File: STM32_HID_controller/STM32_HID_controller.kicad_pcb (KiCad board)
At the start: 2 copper layers, 237.3 x 103.7 mm, 48 parts, among them J1 USB_B_Micro, J2 Conn_01x04_Pin, J3 Conn_01x03_Pin, J5 Conn_01x03_Pin, SW1 SW_SPDT, SW10 SW_Push, SW11 SW_Push, SW14 SW_Push, SW2 SW_Push, SW3 SW_Push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

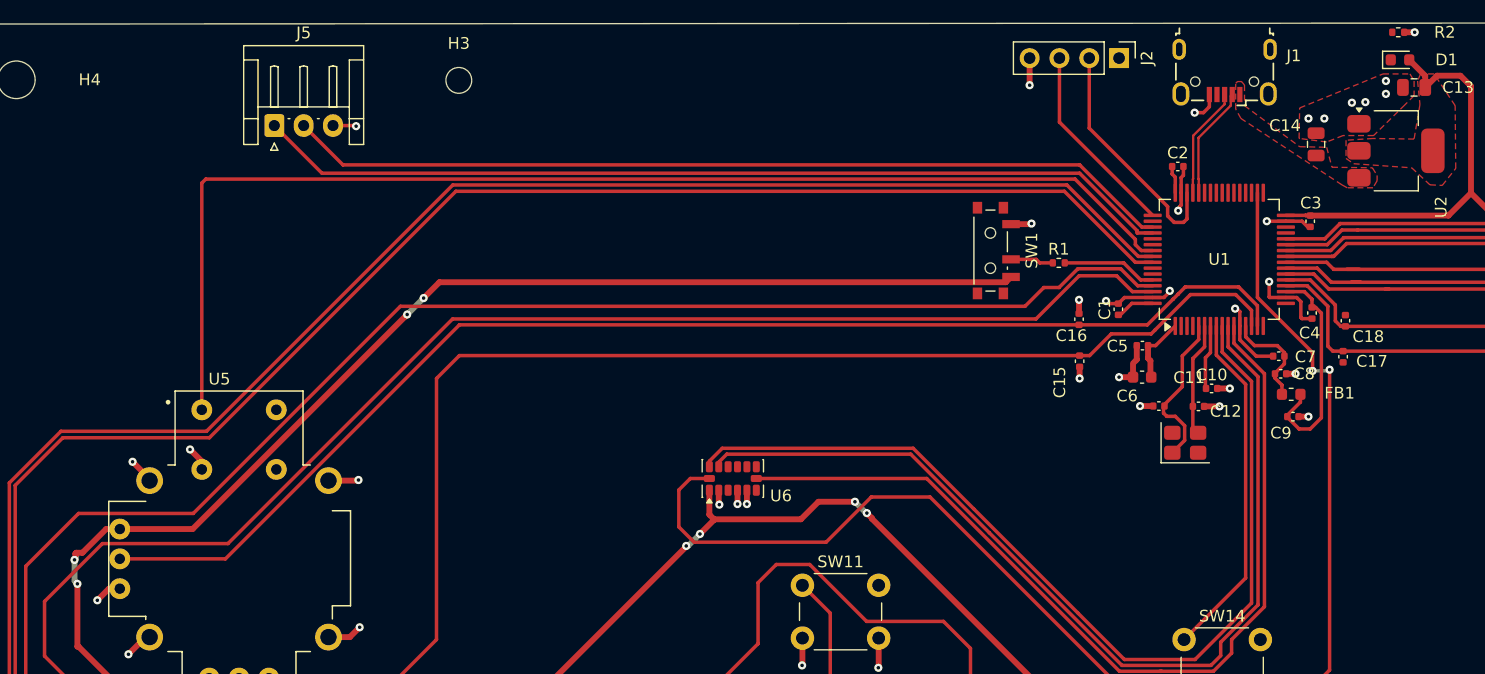
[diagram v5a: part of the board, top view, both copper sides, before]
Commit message: added gnd vias shortend sclk
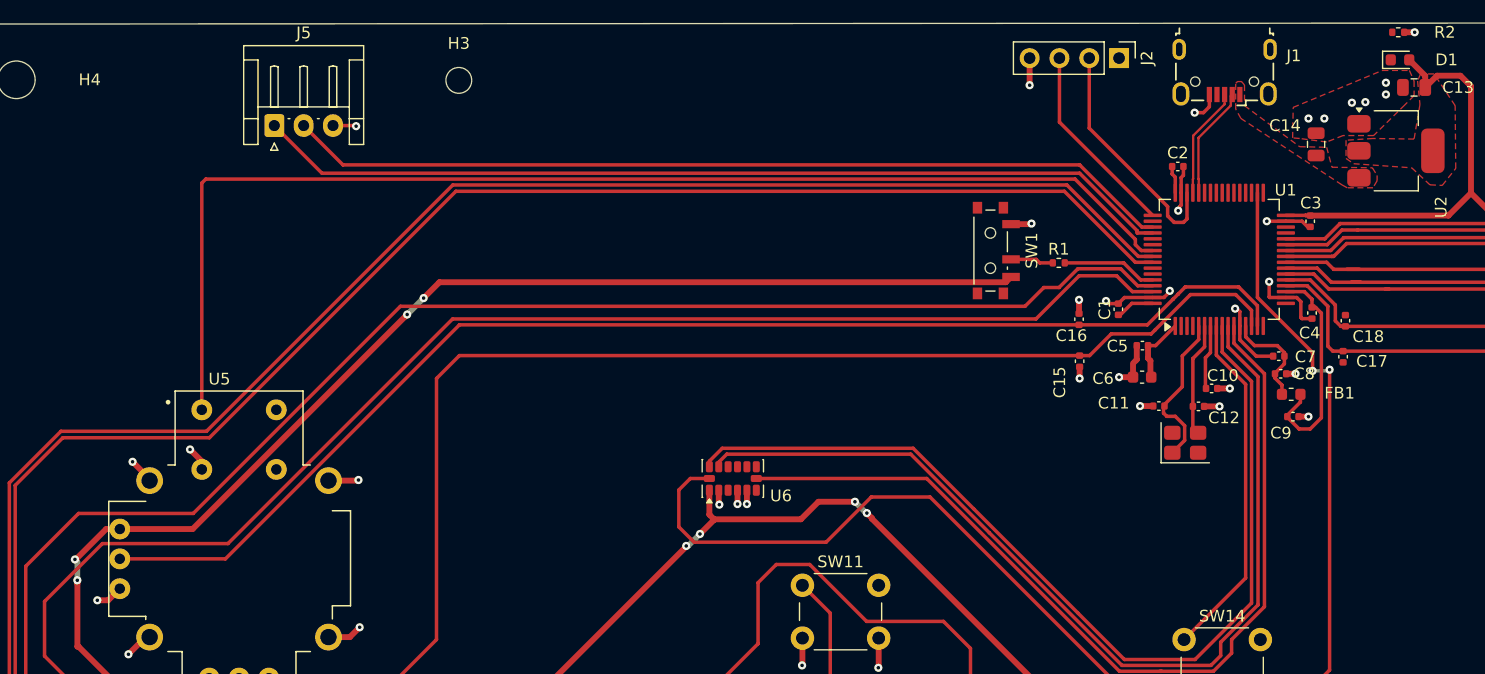
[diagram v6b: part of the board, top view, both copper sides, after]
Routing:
- net +3.3V: track 624.2 -> 623.5 mm
- net GND: track 138.6 -> 138.7 mm, vias 55 -> 61
- net (no net): track 0.10 -> 0.00 mm, vias 6 -> 0
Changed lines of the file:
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@@
 		(tags "capacitor")
 		(property "Reference" "C12"
-			(at 2.321 0.421565 0)
+			(at 2.171 0.971565 0)
 			(layer "F.SilkS")
 			(effects
@@
 		(tags "capacitor")
 		(property "Reference" "C11"
-			(at -2.579 2.424065 0)
+			(at 3.85 0.25 0)
 			(layer "F.SilkS")
 			(effects
@@
 		(tags "capacitor")
 		(property "Reference" "C10"
-			(at 0 -1.16 0)
+			(at 0.95 -1.1 0)
 			(layer "F.SilkS")
 			(effects
@@
 		(tags "capacitor")
 		(property "Reference" "C6"
-			(at 1.275 -1.6 0)
+			(at 3.325 -0.1125 0)
 			(layer "F.SilkS")
 			(effects
@@
 		(tags "LQFP QFP")
 		(property "Reference" "U1"
-			(at 0 0 180)
+			(at 5.9 5.65 180)
 			(layer "F.SilkS")
 			(effects
@@
 		(layer "Edge.Cuts")
 	)
-	(via
-		(at 167.8 23.3)
-		(size 0.7)
-		(drill 0.3)
-		(layers "F.Cu" "B.Cu")
-		(net 0)
-	)
-	(via
-		(at 161.2 25.4)
-		(size 0.7)
-		(drill 0.3)
-		(layers "F.Cu" "B.Cu")
-		(net 0)
-	)
-	(via
-		(at 167.8 22.2)
-		(size 0.7)
-		(drill 0.3)
-		(layers "F.Cu" "B.Cu")
-		(net 0)
-	)
-	(via
-		(at 166.05 24)
-		(size 0.7)
-		(drill 0.3)
-		(layers "F.Cu" "B.Cu")
-		(net 0)
-	)
-	(via
-		(at 162.55 25.4)
-		(size 0.7)
-		(drill 0.3)
-		(layers "F.Cu" "B.Cu")
-		(net 0)
-	)
-	(via
-		(at 164.9 24.05)
-		(size 0.7)
-		(drill 0.3)
-		(layers "F.Cu" "B.Cu")
-		(net 0)
-	)
-	(segment
-		(start 167.8 22.2)
-		(end 167.85 22.2)
-		(width 0.5)
-		(layer "B.Cu")
-		(net 0)
-	)
-	(segment
-		(start 161.15 25.4)
-		(end 161.2 25.4)
-		(width 0.5)
-		(layer "B.Cu")
-		(net 0)
-	)
 	(segment
 		(start 110.95 58.25)
@@
 	)
 	(segment
+		(start 58 66.45)
+		(end 58.925 66.45)
+		(width 0.5)
+		(layer "F.Cu")
+		(net 1)
+	)
+	(segment
 		(start 157.9 40.65)
 		(end 159.275 40.65)
@@
 	)
 	(segment
+		(start 58.925 66.45)
+		(end 59.915 65.46)
+		(width 0.5)
+		(layer "F.Cu")
+		(net 1)
+	)
+	(segment
 		(start 80.1975 56.2525)
 		(end 80.25 56.2)
@@
 	)
 	(segment
-		(start 58.99 65.46)
-		(end 58 66.45)
-		(width 0.5)
-		(layer "F.Cu")
-		(net 1)
-	)
-	(segment
 		(start 151.5 24.9)
 		(end 152.25 24.9)
@@
 	)
 	(segment
+		(start 167.8 23.35)
+		(end 167.8 23.3)
+		(width 0.5)
+		(layer "F.Cu")
+		(net 1)
+	)
+	(segment
 		(start 148.885294 40.65)
 		(end 149.392647 40.142647)
@@
 	)
 	(segment
-		(start 59.915 65.46)
-		(end 58.99 65.46)
-		(width 0.5)
-		(layer "F.Cu")
-		(net 1)
-	)
-	(segment
 		(start 113.35 57.0725)
 		(end 113.35 58.25)
@@
 	)
 	(via
+		(at 167.8 23.35)
+		(size 0.7)
+		(drill 0.3)
+		(layers "F.Cu" "B.Cu")
+		(free yes)
+		(net 1)
+	)
+	(via
 		(at 137.6 34.35)
 		(size 0.7)
@@
 	)
 	(via
+		(at 161.2 25.4)
+		(size 0.7)
+		(drill 0.3)
+		(layers "F.Cu" "B.Cu")
+		(free yes)
+		(net 1)
+	)
+	(via
 		(at 124.55 72.2)
 		(size 0.7)
@@
 	)
 	(via
+		(at 166.05 24)
+		(size 0.7)
+		(drill 0.3)
+		(layers "F.Cu" "B.Cu")
+		(free yes)
+		(net 1)
+	)
+	(via
 		(at 151.5 24.9)
 		(size 0.7)
@@
 	)
 	(via
+		(at 162.55 25.4)
+		(size 0.7)
+		(drill 0.3)
+		(layers "F.Cu" "B.Cu")
+		(free yes)
+		(net 1)
+	)
+	(via
 		(at 143.95 40.95)
 		(size 0.7)
@@
 	)
 	(via
+		(at 164.9 24.05)
+		(size 0.7)
+		(drill 0.3)
+		(layers "F.Cu" "B.Cu")
+		(free yes)
+		(net 1)
+	)
+	(via
 		(at 160.1 47.15)
 		(size 0.7)
@@
 	)
 	(via
+		(at 167.8 22.35)
+		(size 0.7)
+		(drill 0.3)
+		(layers "F.Cu" "B.Cu")
+		(free yes)
+		(net 1)
+	)
+	(via
 		(at 150.6 76.4)
 		(size 0.7)
@@
 	)
 	(segment
-		(start 56.73076 62.4)
-		(end 58.75076 60.38)
+		(start 161.15 25.4)
+		(end 161.2 25.4)
 		(width 0.5)
-		(layer "F.Cu")
-		(net 2)
+		(layer "B.Cu")
+		(net 1)
 	)
 	(segment
@@
 	)
 	(segment
+		(start 56.3 64.75)
+		(end 56.294975 64.744975)
+		(width 0.5)
+		(layer "F.Cu")
+		(net 2)
+	)
+	(segment
 		(start 250.32 97.58)
 		(end 242.8 97.58)
@@
 	)
 	(segment
+		(start 56.3 65.05)
+		(end 56.3 64.75)
+		(width 0.5)
+		(layer "F.Cu")
+		(net 2)
+	)
+	(segment
 		(start 122.555025 58.055025)
 		(end 119.444975 58.055025)
@@
 	)
 	(segment
-		(start 56.130025 62.930025)
-		(end 56.055025 63.005025)
-		(width 0.5)
-		(layer "F.Cu")
-		(net 2)
-	)
-	(segment
 		(start 168.55 74.3)
 		(end 158.65 84.2)
@@
 	)
 	(segment
-		(start 58.75076 60.38)
-		(end 59.915 60.38)
-		(width 0.5)
-		(layer "F.Cu")
-		(net 2)
-	)
-	(segment
 		(start 68.85 82.85)
 		(end 87.2 82.85)
@@
 	)
 	(segment
-		(start 56.2 62.4)
-		(end 56.73076 62.4)
-		(width 0.5)
-		(layer "F.Cu")
-		(net 2)
-	)
-	(segment
-		(start 56.130025 62.469975)
-		(end 56.130025 62.930025)
+		(start 172.15 21.75)
+		(end 174.15 21.75)
 		(width 0.5)
 		(layer "F.Cu")
@@
 	)
 	(segment
-		(start 172.15 21.75)
-		(end 174.15 21.75)
+		(start 56.125735 63.005025)
+		(end 58.75076 60.38)
 		(width 0.5)
 		(layer "F.Cu")
@@
 	)
 	(segment
-		(start 56.2 62.4)
-		(end 56.130025 62.469975)
-		(width 0.5)
-		(layer "F.Cu")
-		(net 2)
-	)
-	(segment
 		(start 173.7 74.3)
 		(end 168.55 74.3)
@@
 	)
 	(segment
+		(start 58.75076 60.38)
+		(end 59.915 60.38)
+		(width 0.5)
+		(layer "F.Cu")
+		(net 2)
+	)
+	(segment
 		(start 173.13 33.67)
 		(end 161.35 33.67)
@@
 	)
 	(via
-		(at 56.3 65.05)
-		(size 0.7)
-		(drill 0.3)
-		(layers "F.Cu" "B.Cu")
-		(net 2)
-	)
-	(via
 		(at 85.8 40.7)
 		(size 0.7)
@@
 	)
 	(via
-		(at 56.055025 63.005025)
+		(at 56.09038 62.96967)
 		(size 0.7)
 		(drill 0.3)
@@
 	)
 	(via
+		(at 56.294975 64.744975)
+		(size 0.7)
+		(drill 0.3)
+		(layers "F.Cu" "B.Cu")
+		(net 2)
+	)
+	(via
 		(at 122.555025 58.055025)
 		(size 0.7)
@@
 	)
 	(segment
-		(start 56.055025 64.805025)
-		(end 56.3 65.05)
+		(start 56.294975 63.174265)
+		(end 56.09038 62.96967)
 		(width 0.5)
 		(layer "B.Cu")
@@
 	)
 	(segment
-		(start 56.055025 63.005025)
-		(end 56.055025 64.805025)
+		(start 56.294975 64.744975)
+		(end 56.294975 63.174265)
 		(width 0.5)
 		(layer "B.Cu")
@@
 	)
 	(segment
-		(start 56.2 62.4)
-		(end 56.2 62.75)
-		(width 0.5)
-		(layer "B.Cu")
-		(net 2)
-	)
-	(segment
 		(start 174.381275 74.381275)
 		(end 174.381275 74.431275)
@@
 		(polygon
 			(pts
-				(xy 160.4 27.1) (xy 160.45 24.5) (xy 167.55 21.6) (xy 169.85 21.6) (xy 170.2 22.2) (xy 170.2 23.45)
+				(xy 159.85 27.05) (xy 159.9 24.45) (xy 167.5 21.3) (xy 169.8 21.3) (xy 170.2 22.2) (xy 170.2 23.45)
 				(xy 169.4 24.25) (xy 166.75 26.85) (xy 164.15 26.85) (xy 162.75 27.4) (xy 160.45 27.1)
 			)

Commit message: added gnd vias shortend sclk
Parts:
- added G***: LOGO, LOGO, F.Cu at (81.8, 112.3)
- moved C9 0.32 mm to (160.0, 50.5), turned to 180 degrees
- moved C4 0.25 mm to (161.4, 42.2)
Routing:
- net +3.3V: track 623.5 -> 742.8 mm, vias 12 -> 18
- net Y: track 64.7 -> 77.2 mm
- net X: track 82.9 -> 95.4 mm
- net B: track 96.3 -> 108.8 mm
- net A: track 110.2 -> 122.7 mm
- net ACC_control: track 29.9 -> 37.3 mm, vias 0 -> 2
- net home: track 273.7 -> 280.2 mm
- net capture: track 237.0 -> 243.5 mm
- net -: track 231.3 -> 237.8 mm
- net +: track 293.3 -> 299.8 mm
- net GND: track 138.7 -> 144.9 mm, vias 61 -> 66
- net /PWR_LED_Cathode: track 0.18 -> 2.58 mm
- net SDI: track 81.2 -> 81.9 mm

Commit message: main pcb finished
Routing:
- net jl: track 103.3 -> 92.0 mm
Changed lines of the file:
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@@
+	)
+	(segment
+		(start 141.310519 30.56052)
+		(end 86.63948 30.56052)
+		(width 0.3)
+		(layer "F.Cu")
+		(net 54)
+	)
+	(segment
+		(start 146.95 36.65)
+		(end 146.45 36.15)
+		(width 0.3)
+		(layer "F.Cu")
+		(net 54)
 	)
 	(segment
@@
 	)
 	(segment
-		(start 66.9 30.9)
+		(start 66.98 50.22)
 		(end 66.9 50.22)
 		(width 0.3)
@@
 	)
 	(segment
-		(start 141.310519 30.56052)
-		(end 67.23948 30.56052)
+		(start 86.63948 30.56052)
+		(end 66.98 50.22)
 		(width 0.3)
 		(layer "F.Cu")
@@
 		(width 0.3)
 		(layer "F.Cu")
-		(net 54)
-	)
-	(segment
-		(start 67.23948 30.56052)
-		(end 66.9 30.9)
-		(width 0.3)
-		(layer "F.Cu")
-		(net 54)
-	)
-	(segment
-		(start 146.95 36.65)
-		(end 146.45 36.15)
-		(width 0.3)
-		(layer "F.Cu")
